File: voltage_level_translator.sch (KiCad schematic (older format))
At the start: 3 parts, among them Q1 DMN6140L

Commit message: update sch and added routed pcb
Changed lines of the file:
@@
 $Descr A4 11693 8268
 encoding utf-8
-Sheet 2 12
+Sheet 5 12
 Title ""
 Date ""
@@
 AR Path="/6145D84A/6137CE63" Ref="Q10"  Part="1"
 AR Path="/614672C1/6137CE63" Ref="Q11"  Part="1"
-F 0 "Q1" V 5999 4300 50  0000 C CNN
+F 0 "Q4" V 5999 4300 50  0000 C CNN
 F 1 "DMN6140L" V 6090 4300 50  0000 C CNN
 F 2 "Package_TO_SOT_SMD:SOT-23" H 5950 4225 50  0001 L CIN
@@
 AR Path="/6145D84A/6137CE6B" Ref="R21"  Part="1"
 AR Path="/614672C1/6137CE6B" Ref="R23"  Part="1"
-F 0 "R3" H 6320 4196 50  0000 L CNN
+F 0 "R9" H 6320 4196 50  0000 L CNN
 F 1 "10k" H 6320 4105 50  0000 L CNN
 F 2 "Resistor_SMD:R_0603_1608Metric_Pad0.98x0.95mm_HandSolder" V 6180 4150 50  0001 C CNN
@@
 AR Path="/6145D84A/6137CE77" Ref="R20"  Part="1"
 AR Path="/614672C1/6137CE77" Ref="R22"  Part="1"
-F 0 "R2" H 5270 4196 50  0000 L CNN
+F 0 "R8" H 5270 4196 50  0000 L CNN
 F 1 "10k" H 5270 4105 50  0000 L CNN
 F 2 "Resistor_SMD:R_0603_1608Metric_Pad0.98x0.95mm_HandSolder" V 5130 4150 50  0001 C CNN

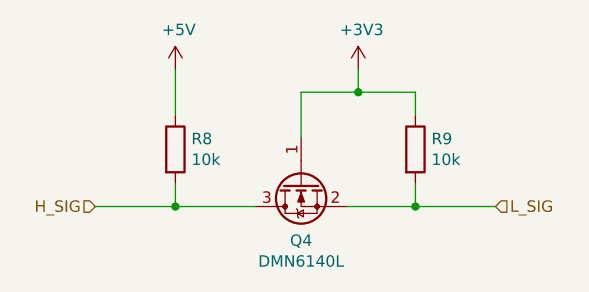
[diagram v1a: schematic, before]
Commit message: remove unncessary parts, update sch
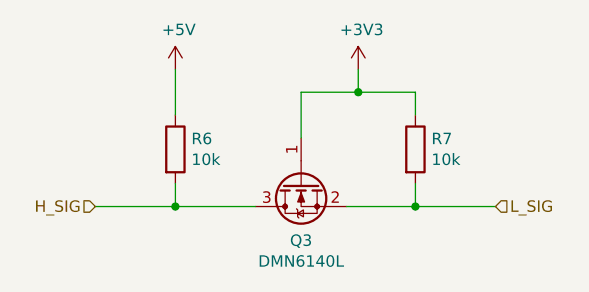
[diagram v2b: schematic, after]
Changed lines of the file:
@@
 $Descr A4 11693 8268
 encoding utf-8
-Sheet 5 12
+Sheet 4 8
 Title ""
 Date ""
@@
 AR Path="/6145D84A/6137CE80" Ref="#PWR0120"  Part="1"
 AR Path="/614672C1/6137CE80" Ref="#PWR0122"  Part="1"
-F 0 "#PWR0122" H 5200 3650 50  0001 C CNN
+F 0 "#PWR0114" H 5200 3650 50  0001 C CNN
 F 1 "+5V" H 5215 3973 50  0000 C CNN
 F 2 "" H 5200 3800 50  0001 C CNN
@@
 AR Path="/6145D84A/6137CE86" Ref="#PWR0121"  Part="1"
 AR Path="/614672C1/6137CE86" Ref="#PWR0123"  Part="1"
-F 0 "#PWR0123" H 6000 3650 50  0001 C CNN
+F 0 "#PWR0115" H 6000 3650 50  0001 C CNN
 F 1 "+3V3" H 6015 3973 50  0000 C CNN
 F 2 "" H 6000 3800 50  0001 C CNN
@@
 AR Path="/6145D84A/6137CE63" Ref="Q10"  Part="1"
 AR Path="/614672C1/6137CE63" Ref="Q11"  Part="1"
-F 0 "Q4" V 5999 4300 50  0000 C CNN
+F 0 "Q3" V 5999 4300 50  0000 C CNN
 F 1 "DMN6140L" V 6090 4300 50  0000 C CNN
 F 2 "Package_TO_SOT_SMD:SOT-23" H 5950 4225 50  0001 L CIN
@@
 AR Path="/6145D84A/6137CE6B" Ref="R21"  Part="1"
 AR Path="/614672C1/6137CE6B" Ref="R23"  Part="1"
-F 0 "R9" H 6320 4196 50  0000 L CNN
+F 0 "R7" H 6320 4196 50  0000 L CNN
 F 1 "10k" H 6320 4105 50  0000 L CNN
 F 2 "Resistor_SMD:R_0603_1608Metric_Pad0.98x0.95mm_HandSolder" V 6180 4150 50  0001 C CNN
@@
 AR Path="/6145D84A/6137CE77" Ref="R20"  Part="1"
 AR Path="/614672C1/6137CE77" Ref="R22"  Part="1"
-F 0 "R8" H 5270 4196 50  0000 L CNN
+F 0 "R6" H 5270 4196 50  0000 L CNN
 F 1 "10k" H 5270 4105 50  0000 L CNN
 F 2 "Resistor_SMD:R_0603_1608Metric_Pad0.98x0.95mm_HandSolder" V 5130 4150 50  0001 C CNN
